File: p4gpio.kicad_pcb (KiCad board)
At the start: 4 copper layers, 87.9 x 23 mm, 94 parts, among them J1 C2760486, J10 Conn_01x04_Socket, J11 Conn_01x04, J2 C2760486, J3 Conn_01x08_Pin, J4 Conn_01x08_Pin, J5 Conn_01x08_Pin, J6 Conn_01x08_Pin, J7 Conn_01x08_Pin, J8 Conn_01x08_Pin, J9 Conn_01x04_Socket, Q1 MBT3906DW1, Q2 AO3401A, Q3 MBT3906DW1, Q4 AO3401A, U1 TLV62569DBV, U3 W25Q128JVS, U4 TLV62569DBV, Y1 40MHz(+-10 ppm) C501798

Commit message: Ordered
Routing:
- net /Minimal P4 V3/VDD_HP: track 56.3 -> 58.7 mm
- net /B2_5: track 20.1 -> 21.5 mm
- net /RESET: track 64.7 -> 65.4 mm
- net /BOOT: track 94.8 -> 95.5 mm
- net /B2_7: track 16.5 -> 17.1 mm

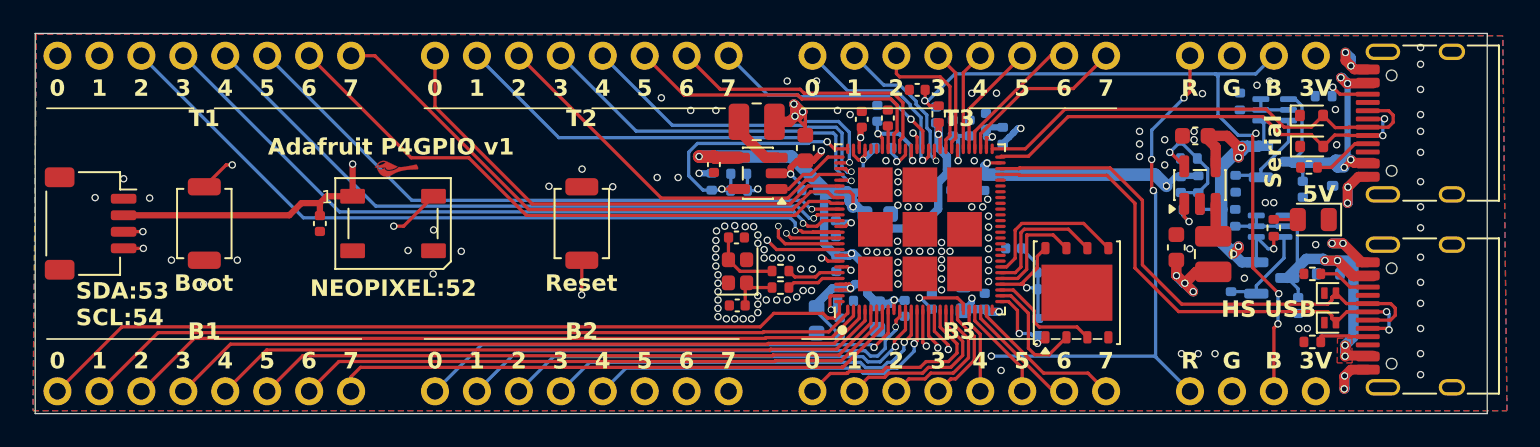
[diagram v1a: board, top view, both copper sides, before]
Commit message: Connect flash VDD and skooch USBs apart. Start of v2
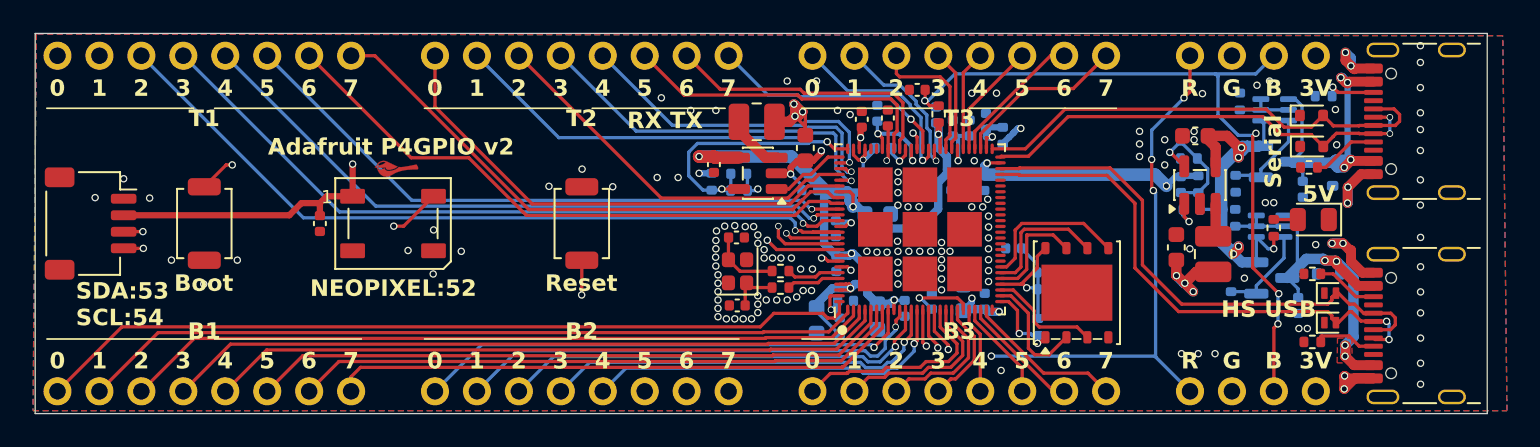
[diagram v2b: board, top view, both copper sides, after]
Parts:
- J1, J2: footprint Connector_USB:USB_C_Receptacle_HRO_TYPE-C-31-M-12 -> Adafruit:USB_C_Receptacle_HRO_TYPE-C-31-M-31
- moved J1 0.58 mm to (207.3, 90.5)
- moved J2 0.11 mm to (207.3, 78.1)
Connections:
- C17 pad 1: /Minimal P4 V3/VDDO_FLASH -> /Minimal P4 V3/VDD_FLASH
- U2 pad 71: /Minimal P4 V3/VDDO_FLASH -> /Minimal P4 V3/VDD_FLASH
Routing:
- net /Minimal P4 V3/VDD_FLASH: track 9.81 -> 34.2 mm, vias 1 -> 2
- net GND: track 18.5 -> 22.5 mm, vias 146 -> 145
- net /Minimal P4 V3/VDDO_FLASH: track 1.39 -> 0.00 mm
- net Net-(J1-CC2): track 3.18 -> 3.76 mm
- net Net-(J1-CC1): track 3.20 -> 3.79 mm
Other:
- board text added: "Adafruit P4GPIO v2"
- board text added: "RX"
- board text added: "TX"
- board text removed: "Adafruit P4GPIO v1"

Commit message: ready for v2
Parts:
- removed the G*** at (144.5, 81.0)
- added G***: LOGO, chickadee:chickadee_2mm_fcu, F.Cu at (126.4, 79.3)
- C17, C18, C27, C29, C30: value 1uF -> 1uF/16V(10%)
- R13: value 2.2K -> 5.1K(1%)
- R14, R209, R210: value 10K -> 10K(1%)
- R200, R28: value 10k -> 10K(1%)
